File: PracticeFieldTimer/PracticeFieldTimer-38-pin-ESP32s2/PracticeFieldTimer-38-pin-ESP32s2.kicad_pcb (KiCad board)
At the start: 2 copper layers, 140.1 x 160 mm, 28 parts, among them J1 External Controls, J2 4 x 20 I2C LCD, J3 Panel, J4 DS3231 Module, J5 /CAN Enable, J6 RJ45, J7 RJ45, J8 CAN Terminate, U1 ESP32-DevKitC, U2 SN65HVD230DR

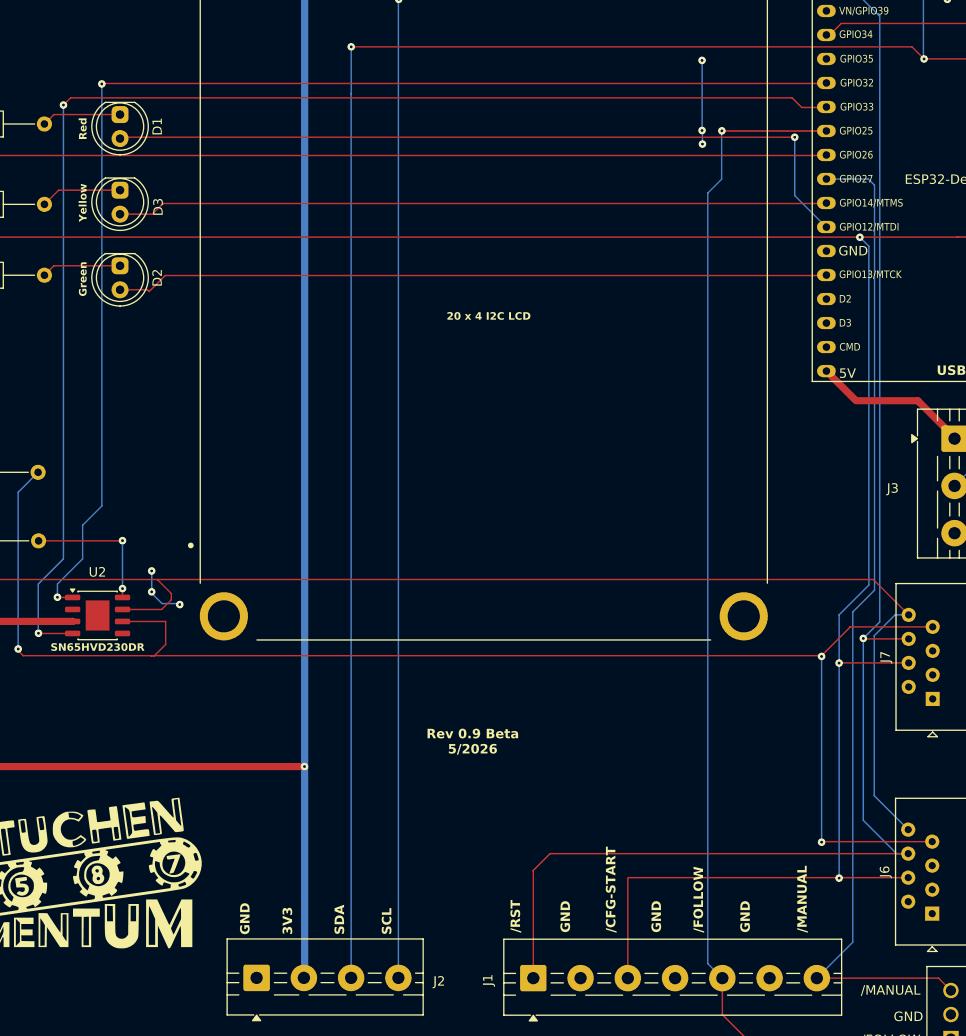
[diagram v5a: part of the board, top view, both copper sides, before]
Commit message: Uncross CAN Transmit and CAN Receive. They were interchanged.
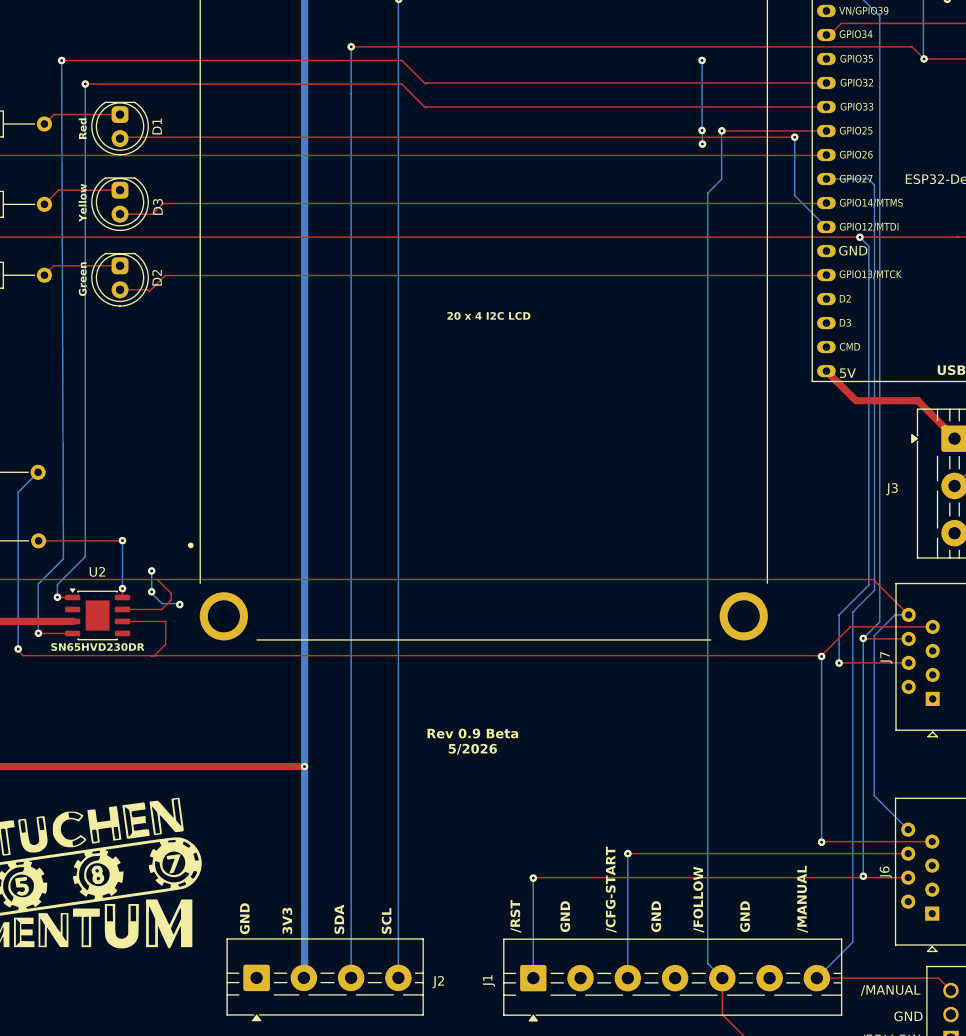
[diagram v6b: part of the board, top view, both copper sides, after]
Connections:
- J6 pad 4: /CFG-START -> /RST
- J6 pad 6: /RST -> /CFG-START
- U1 pad 7: CAN TX -> CAN RX
- U1 pad 8: CAN RX -> CAN TX
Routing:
- net /CFG-START: track 266.7 -> 246.8 mm
- net CAN RX: track 142.4 -> 147.6 mm
- net /RST: track 260.1 -> 258.0 mm, vias 2 -> 4
- net CAN TX: track 134.5 -> 136.6 mm
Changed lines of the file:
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@@
 			(layers "*.Cu" "*.Mask")
 			(remove_unused_layers no)
-			(net 28 "CAN TX")
+			(net 41 "CAN RX")
 			(pinfunction "32K_XP/GPIO32/ADC1_CH4")
 			(pintype "bidirectional")
@@
 			(layers "*.Cu" "*.Mask")
 			(remove_unused_layers no)
-			(net 41 "CAN RX")
+			(net 28 "CAN TX")
 			(pinfunction "32K_XN/GPIO33/ADC1_CH5")
 			(pintype "bidirectional")
@@
 			(layers "*.Cu" "*.Mask")
 			(remove_unused_layers no)
-			(net 10 "{slash}CFG-START")
+			(net 11 "{slash}RST")
 			(pintype "passive")
 		)
@@
 			(layers "*.Cu" "*.Mask")
 			(remove_unused_layers no)
-			(net 11 "{slash}RST")
+			(net 10 "{slash}CFG-START")
 			(pintype "passive")
 		)
@@
 	)
 	(segment
-		(start 128.562263 154.450976)
-		(end 98.980363 154.450976)
+		(start 28.519977 86.685721)
+		(end 133.844663 86.685721)
 		(width 0.1524)
 		(layer "F.Cu")
@@
 	)
 	(segment
-		(start 98.898063 154.462676)
-		(end 98.898063 165.083676)
+		(start 98.810976 151.910976)
+		(end 128.562263 151.910976)
 		(width 0.1524)
 		(layer "F.Cu")
@@
 	)
 	(segment
-		(start 28.519977 86.685721)
-		(end 133.844663 86.685721)
+		(start 121.266524 131.733476)
+		(end 121.25 131.75)
 		(width 0.1524)
 		(layer "F.Cu")
@@
 	)
 	(segment
-		(start 121.266524 131.733476)
-		(end 121.25 131.75)
+		(start 140.435108 86.685721)
+		(end 143.835977 86.685721)
 		(width 0.1524)
 		(layer "F.Cu")
@@
 	)
 	(segment
-		(start 140.435108 86.685721)
-		(end 143.835977 86.685721)
+		(start 98.9 151.910976)
+		(end 98.810976 151.910976)
 		(width 0.1524)
 		(layer "F.Cu")
@@
 	)
 	(via
-		(at 121.25 154.5)
+		(at 98.9 151.910976)
 		(size 0.8)
 		(drill 0.3)
@@
 	)
 	(segment
-		(start 123.45 86.7)
-		(end 124.4 87.65)
+		(start 98.9 151.910976)
+		(end 98.898063 151.998063)
 		(width 0.1524)
 		(layer "B.Cu")
@@
 	)
 	(segment
-		(start 30.937977 55.109721)
-		(end 30.937977 55.184721)
+		(start 123.45 86.7)
+		(end 124.4 87.65)
 		(width 0.1524)
 		(layer "B.Cu")
@@
 	)
 	(segment
-		(start 121.25 131.75)
-		(end 121.25 154.5)
+		(start 30.937977 55.109721)
+		(end 30.937977 55.184721)
 		(width 0.1524)
 		(layer "B.Cu")
@@
 	)
 	(segment
-		(start 123.862463 129.193476)
-		(end 123.811663 129.142676)
-		(width 0.1524)
-		(layer "F.Cu")
-		(net 11)
-	)
-	(segment
-		(start 128.562263 151.910976)
-		(end 90.680163 151.910976)
+		(start 98.898063 151.998063)
+		(end 98.898063 165.083676)
 		(width 0.1524)
-		(layer "F.Cu")
-		(net 11)
+		(layer "B.Cu")
+		(net 10)
 	)
 	(segment
-		(start 90.680163 151.910976)
-		(end 88.886663 153.704476)
+		(start 123.862463 129.193476)
+		(end 123.811663 129.142676)
 		(width 0.1524)
 		(layer "F.Cu")
@@
 	)
 	(segment
-		(start 128.612263 129.193476)
-		(end 123.862463 129.193476)
-		(width 0.1524)
-		(layer "F.Cu")
-		(net 11)
-	)
-	(segment
-		(start 88.886663 153.704476)
-		(end 88.898063 153.715876)
+		(start 128.562263 154.450976)
+		(end 89.149024 154.450976)
 		(width 0.1524)
 		(layer "F.Cu")
@@
 	)
 	(segment
-		(start 88.898063 153.715876)
-		(end 88.898063 165.083676)
+		(start 128.612263 129.193476)
+		(end 123.862463 129.193476)
 		(width 0.1524)
 		(layer "F.Cu")
@@
 	)
 	(via
+		(at 88.9 154.5)
+		(size 0.8)
+		(drill 0.3)
+		(layers "F.Cu" "B.Cu")
+		(net 11)
+	)
+	(via
 		(at 123.811663 129.142676)
 		(size 0.8)
@@
 	)
 	(via
-		(at 117.461663 42.503276)
+		(at 123.811663 154.3)
 		(size 0.8)
 		(drill 0.3)
@@
 		(net 11)
 	)
-	(segment
-		(start 127.326763 151.910976)
-		(end 128.562263 151.910976)
-		(width 0.1524)
-		(layer "B.Cu")
+	(via
+		(at 117.461663 42.503276)
+		(size 0.8)
+		(drill 0.3)
+		(layers "F.Cu" "B.Cu")
 		(net 11)
 	)
@@
 	)
 	(segment
+		(start 88.9 154.6)
+		(end 88.898063 154.601937)
+		(width 0.1524)
+		(layer "B.Cu")
+		(net 11)
+	)
+	(segment
 		(start 119.807577 57.729721)
 		(end 119.553577 57.475721)
@@
 	)
 	(segment
-		(start 123.811663 129.142676)
-		(end 123.811663 148.395876)
+		(start 123.811663 154.3)
+		(end 123.811663 129.142676)
 		(width 0.1524)
 		(layer "B.Cu")
@@
 	)
 	(segment
+		(start 88.898063 154.601937)
+		(end 88.898063 165.083676)
+		(width 0.1524)
+		(layer "B.Cu")
+		(net 11)
+	)
+	(segment
 		(start 125.480256 63.25)
 		(end 125.55 63.25)
@@
 	)
 	(segment
-		(start 123.811663 148.395876)
-		(end 127.326763 151.910976)
-		(width 0.1524)
-		(layer "B.Cu")
-		(net 11)
-	)
-	(segment
 		(start 119.553577 57.475721)
 		(end 119.705977 57.475721)
@@
 	)
 	(segment
+		(start 88.9 154.5)
+		(end 88.9 154.6)
+		(width 0.1524)
+		(layer "B.Cu")
+		(net 11)
+	)
+	(segment
 		(start 108.898063 165.083676)
 		(end 108.898063 168.940676)
@@
 	)
 	(segment
+		(start 77.5 73)
+		(end 77.581079 72.918921)
+		(width 0.1524)
+		(layer "F.Cu")
+		(net 28)
+	)
+	(segment
+		(start 75 70.5)
+		(end 77.5 73)
+		(width 0.1524)
+		(layer "F.Cu")
+		(net 28)
+	)
+	(segment
 		(start 38.576977 124.809721)
 		(end 38.552977 124.785721)
@@
 	)
 	(segment
-		(start 43.251977 70.556721)
-		(end 43.378977 70.429721)
+		(start 43.271456 70.5)
+		(end 75 70.5)
 		(width 0.1524)
 		(layer "F.Cu")
@@
 	)
 	(segment
-		(start 43.378977 70.429721)
-		(end 119.937977 70.429721)
+		(start 41.5 70.484809)
+		(end 43.271456 70.5)
+		(width 0.1524)
+		(layer "F.Cu")
+		(net 28)
+	)
+	(segment
+		(start 77.581079 72.918921)
+		(end 119.909177 72.918921)
 		(width 0.1524)
 		(layer "F.Cu")
@@
 	)
 	(via
-		(at 43.251977 70.480521)
+		(at 41.5 70.484809)
 		(size 0.8)
 		(drill 0.3)
@@
 	)
 	(segment
-		(start 41.219977 120.721721)
-		(end 41.219977 117.165721)
+		(start 41.5 70.484809)
+		(end 41.5 120.5)
 		(width 0.1524)
 		(layer "B.Cu")
@@
 	(segment
 		(start 38.552977 124.785721)
-		(end 38.552977 123.388721)
+		(end 38.552977 123.447023)
 		(width 0.1524)
 		(layer "B.Cu")
@@
 	)
 	(segment
-		(start 38.552977 123.388721)
-		(end 41.219977 120.721721)
+		(start 38.552977 123.447023)
+		(end 41.5 120.5)
 		(width 0.1524)
 		(layer "B.Cu")
@@
 	)
 	(segment
-		(start 43.251977 115.133721)
-		(end 43.251977 70.556721)
-		(width 0.1524)
-		(layer "B.Cu")
-		(net 28)
-	)
-	(segment
-		(start 41.219977 117.165721)
-		(end 43.251977 115.133721)
-		(width 0.1524)
-		(layer "B.Cu")
-		(net 28)
-	)
-	(segment
-		(start 116.276977 71.953721)
-		(end 117.292977 72.969721)
+		(start 75 68)
+		(end 39 68)
 		(width 0.1524)
 		(layer "F.Cu")
@@
 	)
 	(segment
-		(start 39.187977 72.715721)
-		(end 39.949977 71.953721)
+		(start 77.5 70.5)
+		(end 75 68)
 		(width 0.1524)
 		(layer "F.Cu")
@@
 	)
 	(segment
-		(start 39.949977 71.953721)
-		(end 116.276977 71.953721)
+		(start 36.570377 128.619721)
+		(end 36.546377 128.595721)
 		(width 0.1524)
 		(layer "F.Cu")
@@
 	)
 	(segment
-		(start 36.570377 128.619721)
-		(end 36.546377 128.595721)
+		(start 119.909177 70.378921)
+		(end 77.621079 70.378921)
 		(width 0.1524)
 		(layer "F.Cu")
@@
 	)
 	(segment
-		(start 117.292977 72.969721)
-		(end 119.937977 72.969721)
+		(start 77.621079 70.378921)
+		(end 77.5 70.5)
 		(width 0.1524)
 		(layer "F.Cu")
@@
 	)
 	(via
-		(at 39.187977 72.715721)
+		(at 39 68)
 		(size 0.8)
 		(drill 0.3)
@@
 	)
 	(segment
-		(start 36.520977 123.388721)
-		(end 36.520977 128.570321)
+		(start 39 68)
+		(end 39.187977 120.721721)
 		(width 0.1524)
 		(layer "B.Cu")
@@
 	)
 	(segment
-		(start 39.187977 120.721721)
-		(end 36.520977 123.388721)
+		(start 36.520977 128.570321)
+		(end 36.546377 128.595721)
 		(width 0.1524)
 		(layer "B.Cu")
@@
 	)
 	(segment
-		(start 39.187977 72.715721)
-		(end 39.187977 120.721721)
+		(start 39.187977 120.721721)
+		(end 36.520977 123.388721)
 		(width 0.1524)
 		(layer "B.Cu")
@@
 	)
 	(segment
-		(start 36.520977 128.570321)
-		(end 36.546377 128.595721)
+		(start 36.520977 123.388721)
+		(end 36.520977 128.570321)
 		(width 0.1524)
 		(layer "B.Cu")
